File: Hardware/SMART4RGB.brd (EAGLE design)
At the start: 40 x 50 mm, 14 parts, among them IC1 WS2811-SOP8, IC2 WS2811-SOP8, IC3 WS2811-SOP8, IC4 WS2811-SOP8, SW1 QG16F-RGB, SW2 QG16F-RGB, SW3 QG16F-RGB, SW4 QG16F-RGB

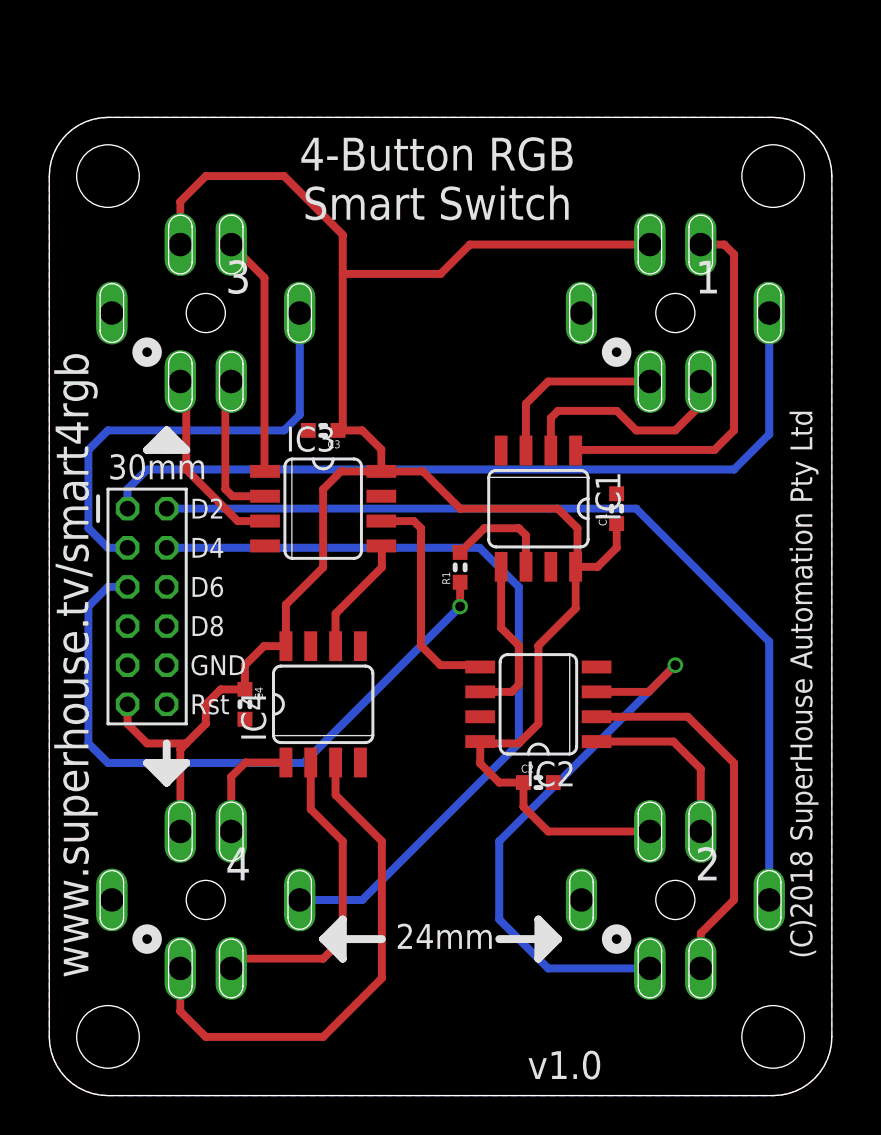
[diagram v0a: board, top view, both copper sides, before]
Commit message: Alter size of board and hole locations to match updated controller. Switch green and blue connections to make colours match WS2812 profile.
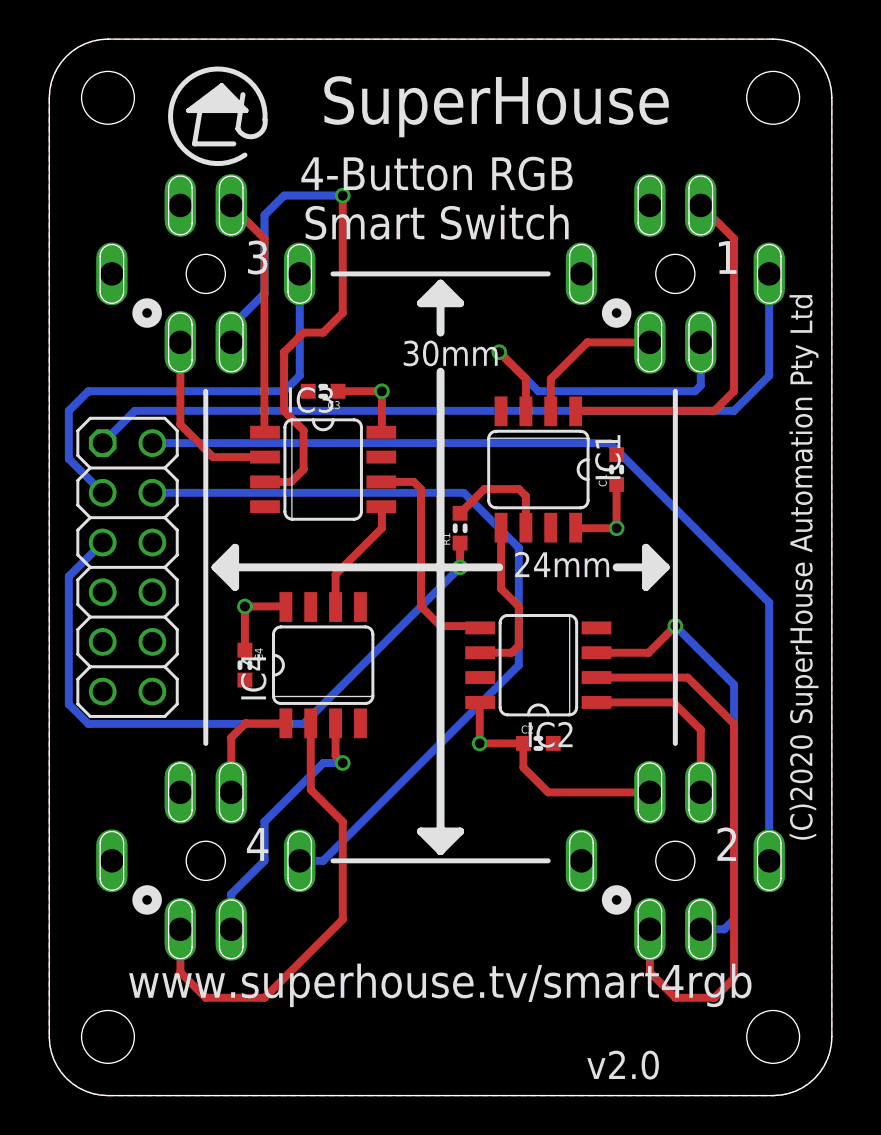
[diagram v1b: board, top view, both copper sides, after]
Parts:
- C1, C2, C3, C4: device freetronics-jon:0603 -> SuperHouse-DiscreteSemi:C0603
- H1: value M06X22MM -> M02X6-SOCKET; device freetronics-jon:2X6-2MM -> SuperHouse-Connectors:2X06-S
- IC1, IC2, IC3, IC4: device freetronics-jon:SO08-SKINNYPADS -> SuperHouse-ICs:SO08-SKINNYPADS
- R1: device freetronics-jon:0603 -> SuperHouse-DiscreteSemi:R0603
- SW1, SW2, SW3, SW4: device freetronics-jon:QG16F-RGB -> SuperHouse-Switches:QG16F-RGB
- moved H1 3.00 mm to (4.00, 27.0), turned to 270 degrees
- moved C1 2.00 mm to (29.0, 32.0)
- moved C2 2.00 mm to (25.0, 18.0)
- moved C3 2.00 mm to (14.0, 36.0)
- moved C4 2.00 mm to (10.0, 22.0)
- moved IC1 2.00 mm to (25.0, 32.0)
- moved IC2 2.00 mm to (25.0, 22.0)
- moved IC3 2.00 mm to (14.0, 32.0)
- moved IC4 2.00 mm to (14.0, 22.0)
- moved R1 2.00 mm to (21.0, 29.0)
- moved SW1 2.00 mm to (32.0, 42.0)
- moved SW2 2.00 mm to (32.0, 12.0)
- moved SW3 2.00 mm to (8.00, 42.0)
- moved SW4 2.00 mm to (8.00, 12.0)
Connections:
- net LED1B: now also SW1.G; no longer SW1.B
- net LED1G: now also SW1.B; no longer SW1.G
- net LED2B: now also SW2.G; no longer SW2.B
- net LED2G: now also SW2.B; no longer SW2.G
- net LED3B: now also SW3.G; no longer SW3.B
- net LED3G: now also SW3.B; no longer SW3.G
- net LED4B: now also SW4.G; no longer SW4.B
- net LED4G: now also SW4.B; no longer SW4.G
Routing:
- net 5V: track 113.3 -> 25.7 mm, vias 0 -> 4
- net LED3B: track 9.74 -> 30.1 mm, vias 0 -> 1
- net LED4B: track 26.3 -> 13.6 mm, vias 0 -> 1
- net LED2G: track 19.2 -> 28.5 mm
- net LED1B: track 9.20 -> 17.0 mm, vias 0 -> 1
- net LED4G: track 16.0 -> 23.4 mm
- net LED2B: track 30.1 -> 22.7 mm
- net LED1G: track 11.6 -> 7.50 mm
- net LED3G: track 7.80 -> 9.22 mm
- net DATA_2: track 46.8 -> 48.1 mm
- net LED1R: track 19.4 -> 18.7 mm
- net DATA_5: track 33.4 -> 34.0 mm
- net DATA_3: track 23.2 -> 22.7 mm
- added copper zone on layer 16, net 5V
- removed copper zone on layer 16, net GND
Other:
- board size 40 x 50 mm -> 40 x 54 mm
- board text added: "(C)2020 SuperHouse Automation Pty Ltd"
- board text added: "SuperHouse"
- board text added: "v2.0"
- board text removed: "(C)2018 SuperHouse Automation Pty Ltd"
- board text removed: "D2"
- board text removed: "D4"
- board text removed: "D6"
- board text removed: "D8"
- board text removed: "GND"
- board text removed: "Rst"
- board text removed: "v1.0"

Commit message: Converted switch isolation from FETs to diodes for v2.1 release.
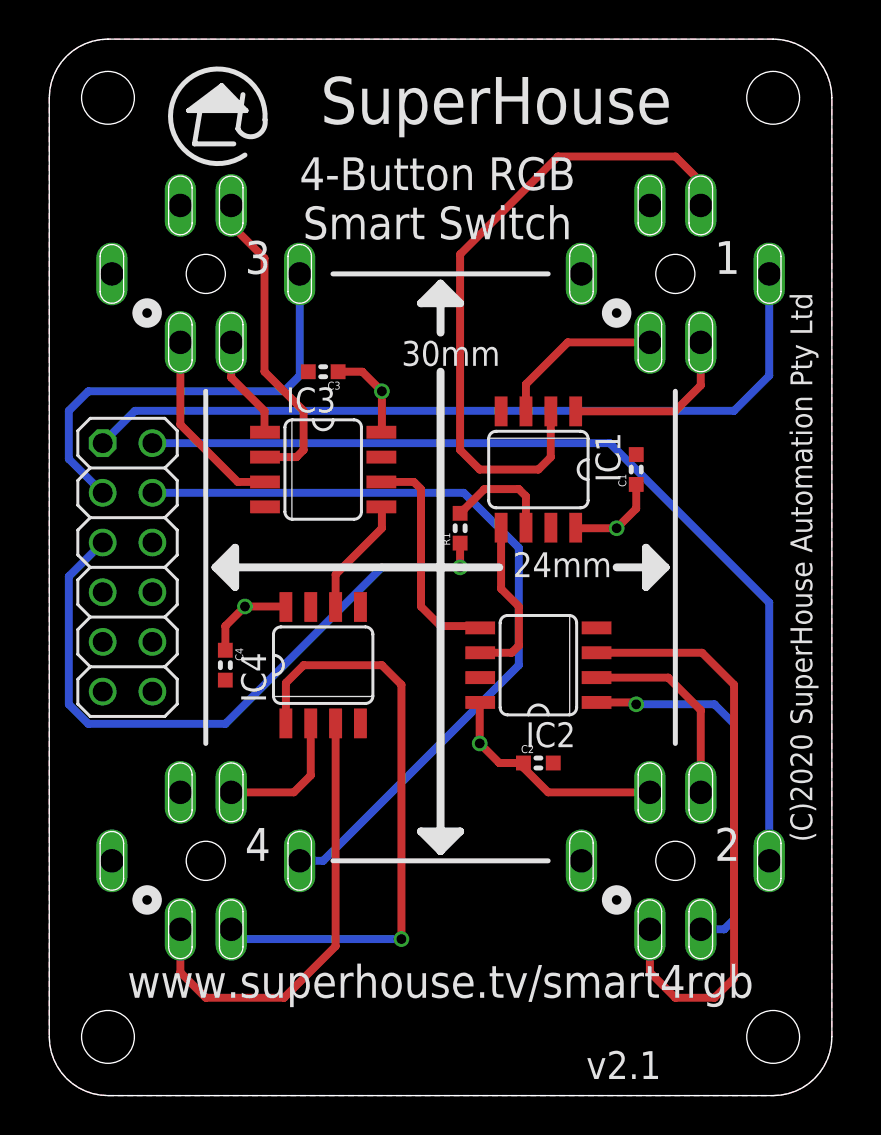
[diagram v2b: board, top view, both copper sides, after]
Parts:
- moved C1 1.00 mm to (30.0, 32.0)
- moved C2 1.00 mm to (25.0, 17.0)
- moved C3 1.00 mm to (14.0, 37.0)
- moved C4 1.00 mm to (9.00, 22.0)
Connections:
- net LED1B: now also SW1.B; no longer SW1.G
- net LED1G: now also IC1.1, SW1.G; no longer IC1.2, SW1.B
- net LED1R: now also IC1.2; no longer IC1.1
- net LED2B: now also SW2.B; no longer SW2.G
- net LED2G: now also IC2.1, SW2.G; no longer IC2.2, SW2.B
- net LED2R: now also IC2.2; no longer IC2.1
- net LED3B: now also SW3.B; no longer SW3.G
- net LED3G: now also IC3.1, SW3.G; no longer IC3.2, SW3.B
- net LED3R: now also IC3.2; no longer IC3.1
- net LED4B: now also SW4.B; no longer SW4.G
- net LED4G: now also IC4.1, SW4.G; no longer IC4.2, SW4.B
- net LED4R: now also IC4.2; no longer IC4.1
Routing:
- net LED3B: track 30.1 -> 9.74 mm, vias 1 -> 0
- net LED1R: track 18.7 -> 33.8 mm
- net LED4B: track 13.6 -> 23.2 mm, vias 1 -> 0
- net LED2G: track 28.5 -> 19.4 mm, vias 0 -> 1
- net LED1B: track 17.0 -> 8.61 mm, vias 1 -> 0
- net LED2B: track 22.7 -> 30.2 mm, vias 1 -> 0
- net LED4G: track 23.4 -> 30.7 mm, vias 0 -> 1
- net LED3G: track 9.22 -> 5.31 mm
- net LED3R: track 12.3 -> 16.2 mm
- net LED1G: track 7.50 -> 9.14 mm
- net LED4R: track 5.90 -> 7.08 mm
- net LED2R: track 9.10 -> 10.2 mm
- net 5V: track 25.7 -> 26.3 mm
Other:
- board text added: "v2.1"
- board text removed: "v2.0"
